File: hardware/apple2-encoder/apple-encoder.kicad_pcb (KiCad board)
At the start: 2 copper layers, 88.9 x 132.1 mm, 49 parts, among them J1 Apple 2, J10 Keyboard, J2 Apple 1, J3 UART, J4 Outputs, J5 SOL-20, J6 Programming, J7 Custom Connector 1 / Proto, J8 Apple II Matrix, SW1 Options, U1 ATmega2560-16AU, Y1 16.000 MHz

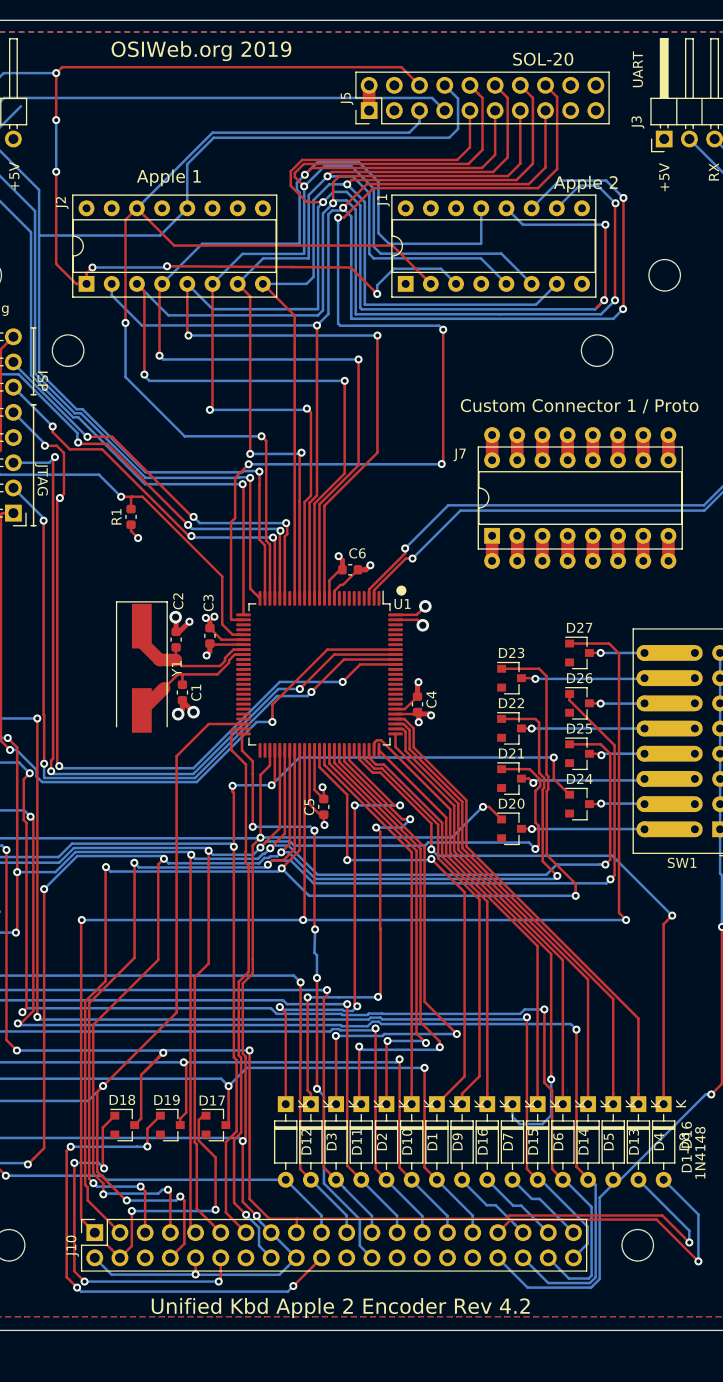
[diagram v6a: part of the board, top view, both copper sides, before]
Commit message: Fix shunted diode footprints on encoder boards
The encoder boards (ATmega328P, Atmega2560, Apple2(2560) can accomodate
keyboard matrices with no diodes, by adding per-row diodes on the
encoder board.  For keyboards with per-key diodes (the typical use
case), the per-row diodes are not needed, and therefore the footprints
should be shunted by default, using a special shunted diode footprint.
When diodes are installed, the shunt can be cut with an x-acto knife.
Previous board revs had the correct footprint, but somehow the regular
diode footprint was substituted on the last release of each of these
PCBS.  The correct footprint has been restored.
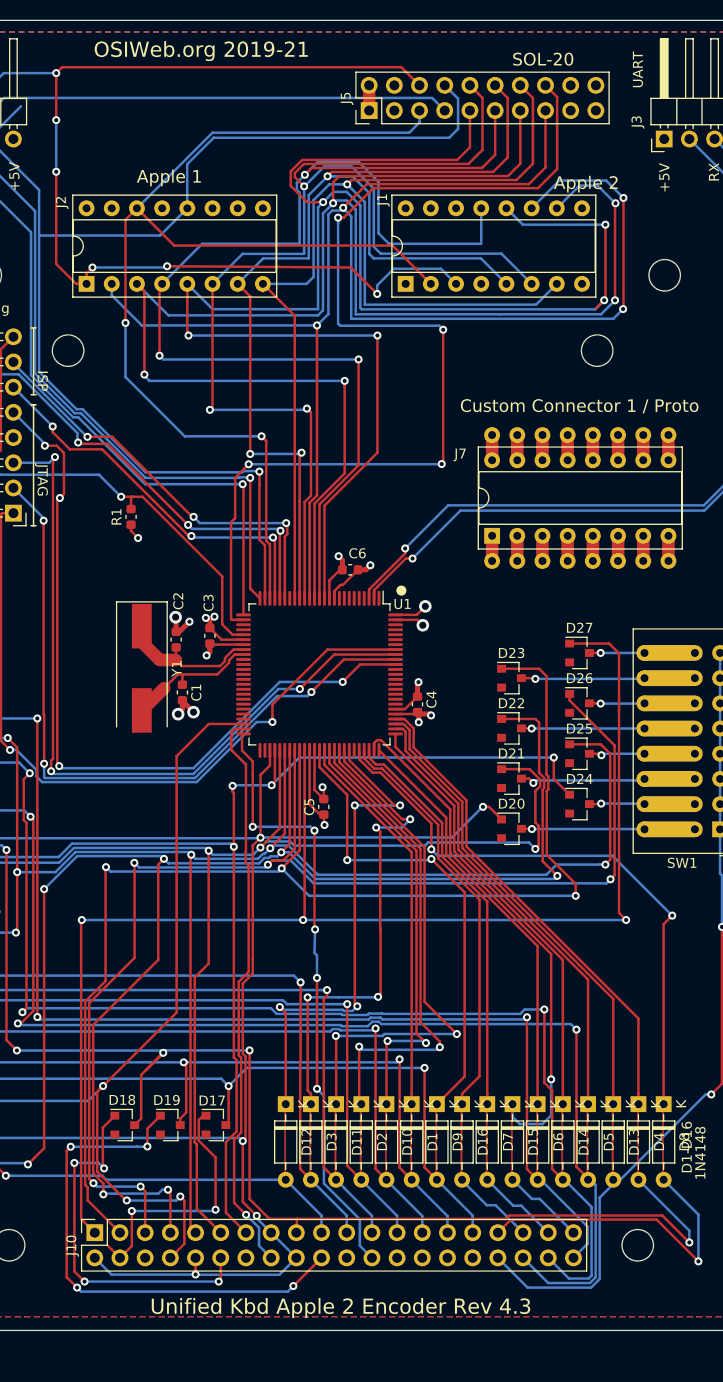
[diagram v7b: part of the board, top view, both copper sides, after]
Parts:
- D1, D10, D11, D12, D13, D14, D15, D16, D2, D3, D4, D5, D6, D7, D8, D9: footprint Diode_THT:D_DO-35_SOD27_P7.62mm_Horizontal -> unikbd:D_DO-35_SOD27_P7.62mm_Horizontal_bypassed
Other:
- board text added: "OSIWeb.org 2019-21"
- board text added: "Unified Kbd Apple 2 Encoder Rev 4.3"
- board text removed: "OSIWeb.org 2019"
- board text removed: "Unified Kbd Apple 2 Encoder Rev 4.2"
